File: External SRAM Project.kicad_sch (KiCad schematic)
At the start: 0 parts

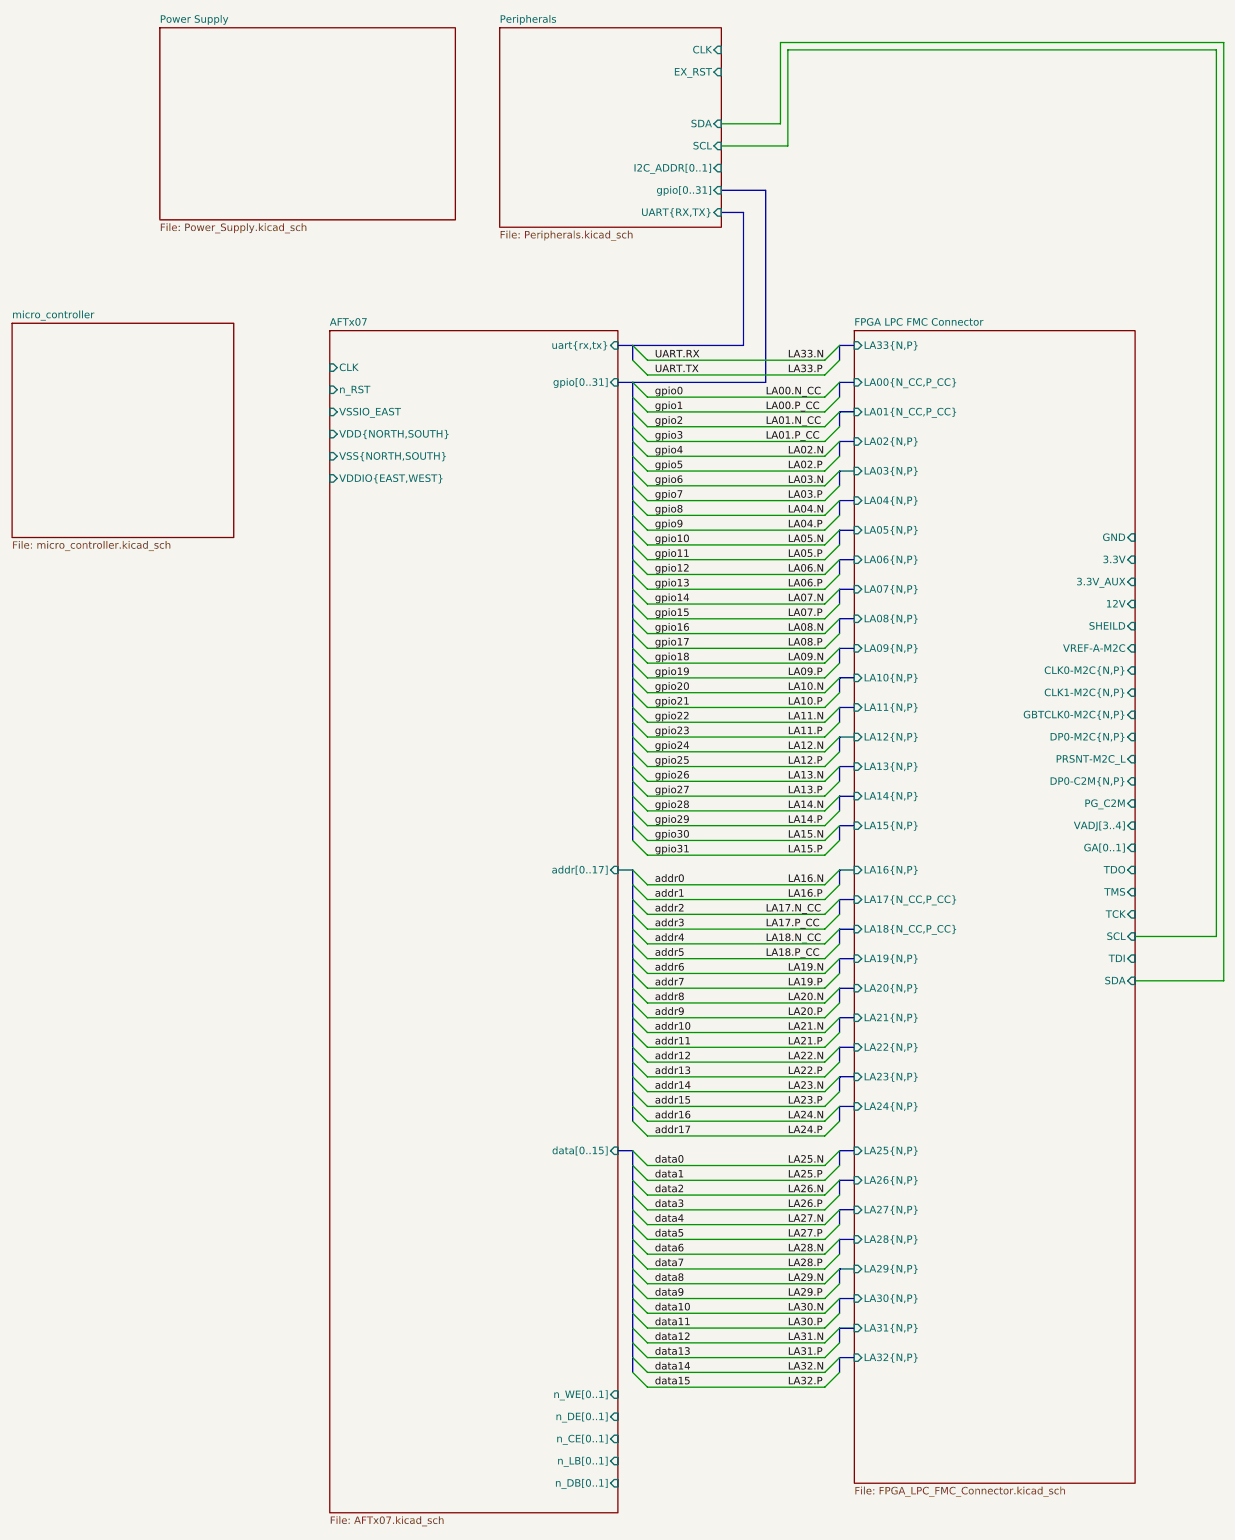
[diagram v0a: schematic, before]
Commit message: fixed some errors and wired clk and nrst
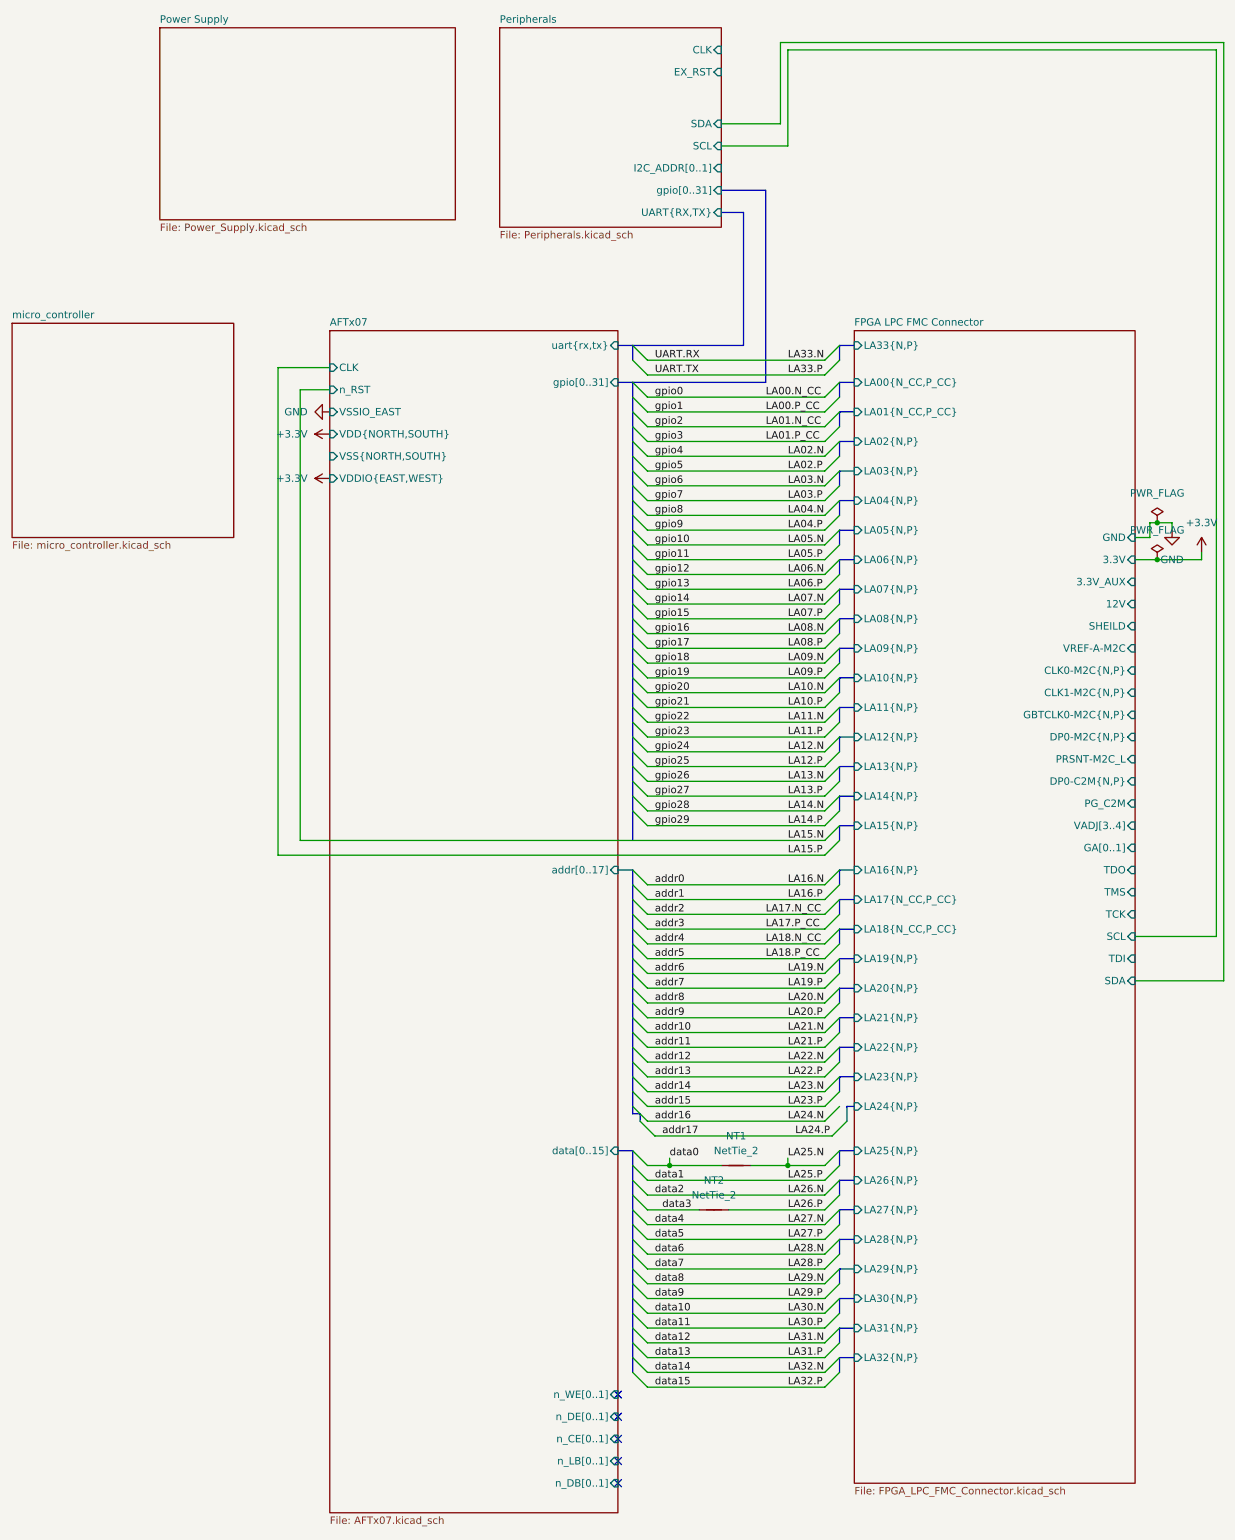
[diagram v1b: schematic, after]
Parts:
- added NT1, NT2: NetTie_2, symbol Device:NetTie_2
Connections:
- net LA25.N: now also NT1.2
- net LA26.P: now also NT2.2
- new net data0: NT1.1
- new net data3: NT2.1
- no-connect marks 0 -> 5
